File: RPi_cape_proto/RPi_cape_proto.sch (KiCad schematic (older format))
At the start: 78 parts, among them J1 Conn_01x04, J10 Conn_01x02, J11 Conn_01x02, J12 Conn_01x02, J15 Conn_01x06, J16 Conn_01x06, J2 Conn_02x20_Odd_Even, J21 Conn_01x06, J3 Conn_01x02, J4 Conn_01x02, J5 Conn_02x20_Odd_Even, J7 Conn_01x02, J8 Conn_02x20_Odd_Even, J9 Conn_01x02, Q2 MMBT3904, Q3 MMBT3904, U2 ADC128D818, U3 ADC128D818

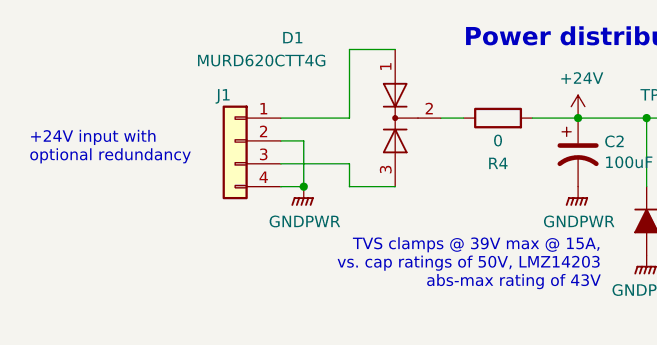
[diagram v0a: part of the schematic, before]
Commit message: Input ORing-diode details
Changed part number and improved heatsinking for input power OR-ing diode
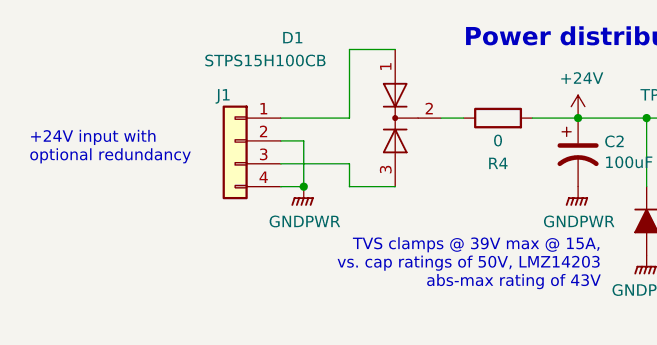
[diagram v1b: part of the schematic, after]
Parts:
- D1: value MURD620CTT4G -> STPS15H100CB; Manufacturer ON Semiconductor -> ST; Part Number MURD620CTT4G -> STPS15H100CB
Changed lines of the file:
@@
 F2 "In_RPi" I L 13850 7950 50
 F3 "In_CPLD" I L 13850 8050 50
-F5 "~Bat_On" O L 13850 7600 50
+F4 "~Bat_On" O L 13850 7600 50
 $EndSheet
 $Comp
@@
 P 2150 950
 F 0 "D1" V 1800 1350 50  0000 L CNN
-F 1 "MURD620CTT4G" V 1900 1250 50  0000 L CNN
+F 1 "STPS15H100CB" V 1900 1250 50  0000 L CNN
 F 2 "Package_TO_SOT_SMD:TO-252-2" H 2150 950 50  0001 C CNN
 F 3 "~" H 2150 950 50  0001 C CNN
-F 4 "ON Semiconductor" V 2150 950 50  0001 C CNN "Manufacturer"
-F 5 "MURD620CTT4G" V 2150 950 50  0001 C CNN "Part Number"
+F 4 "ST" V 2150 950 50  0001 C CNN "Manufacturer"
+F 5 "STPS15H100CB" V 2150 950 50  0001 C CNN "Part Number"
 	1    2150 950
 	0    -1   1    0

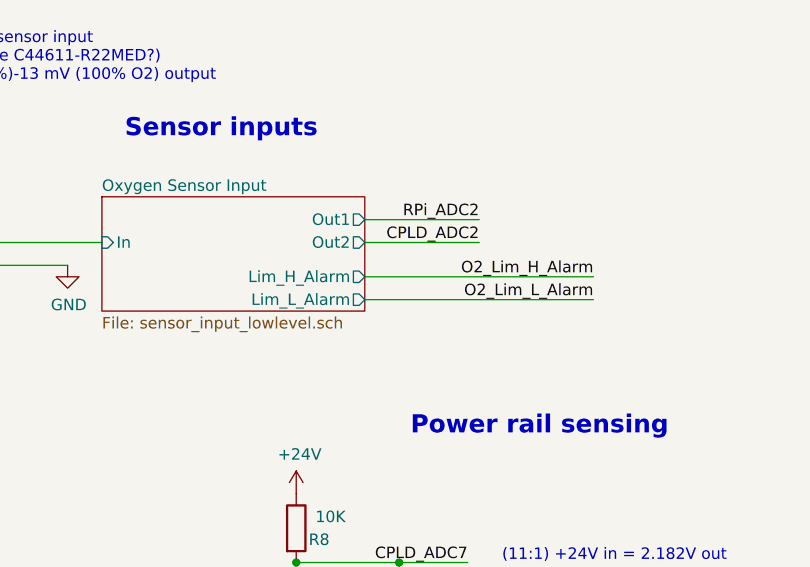
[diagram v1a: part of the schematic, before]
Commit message: Cleanup, manufacturing
Added doc on differences between 'proto' version and 'full' version
Added manufacturing README in proto version
Removed unused hardwired-limited O2 alarm nets in proto version
Fixed missed-annotation on D1 in full version
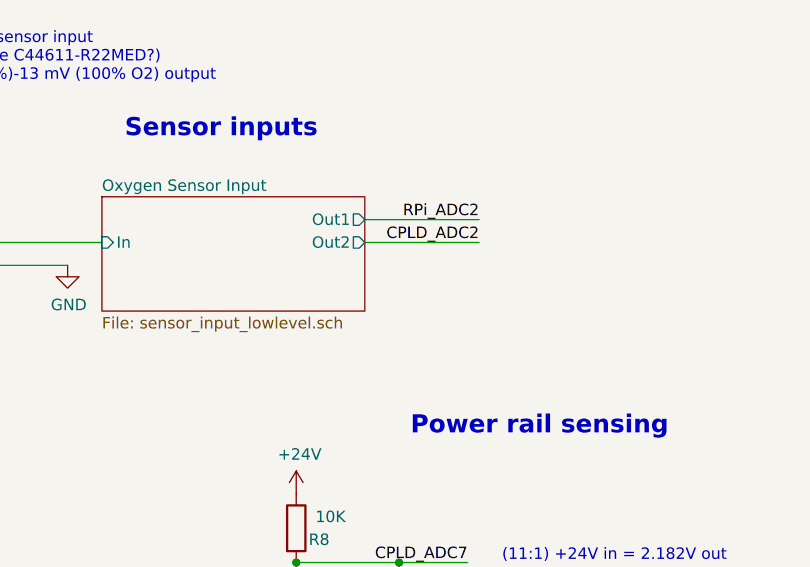
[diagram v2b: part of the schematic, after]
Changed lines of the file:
@@
 F3 "Out1" O R 2550 8200 50
 F4 "Out2" O R 2550 8300 50
-F5 "Lim_H_Alarm" O R 2550 8450 50
-F6 "Lim_L_Alarm" O R 2550 8550 50
 $EndSheet
 $Sheet
@@
 Text Label 10300 2550 0    50   ~ 0
 RPi_SCL
-Text Label 3550 8450 2    50   ~ 0
-O2_Lim_H_Alarm
-Text Label 3550 8550 2    50   ~ 0
-O2_Lim_L_Alarm
-Wire Wire Line
-	2550 8450 3550 8450
-Wire Wire Line
-	2550 8550 3550 8550
 Wire Wire Line
 	8750 7900 7950 7900

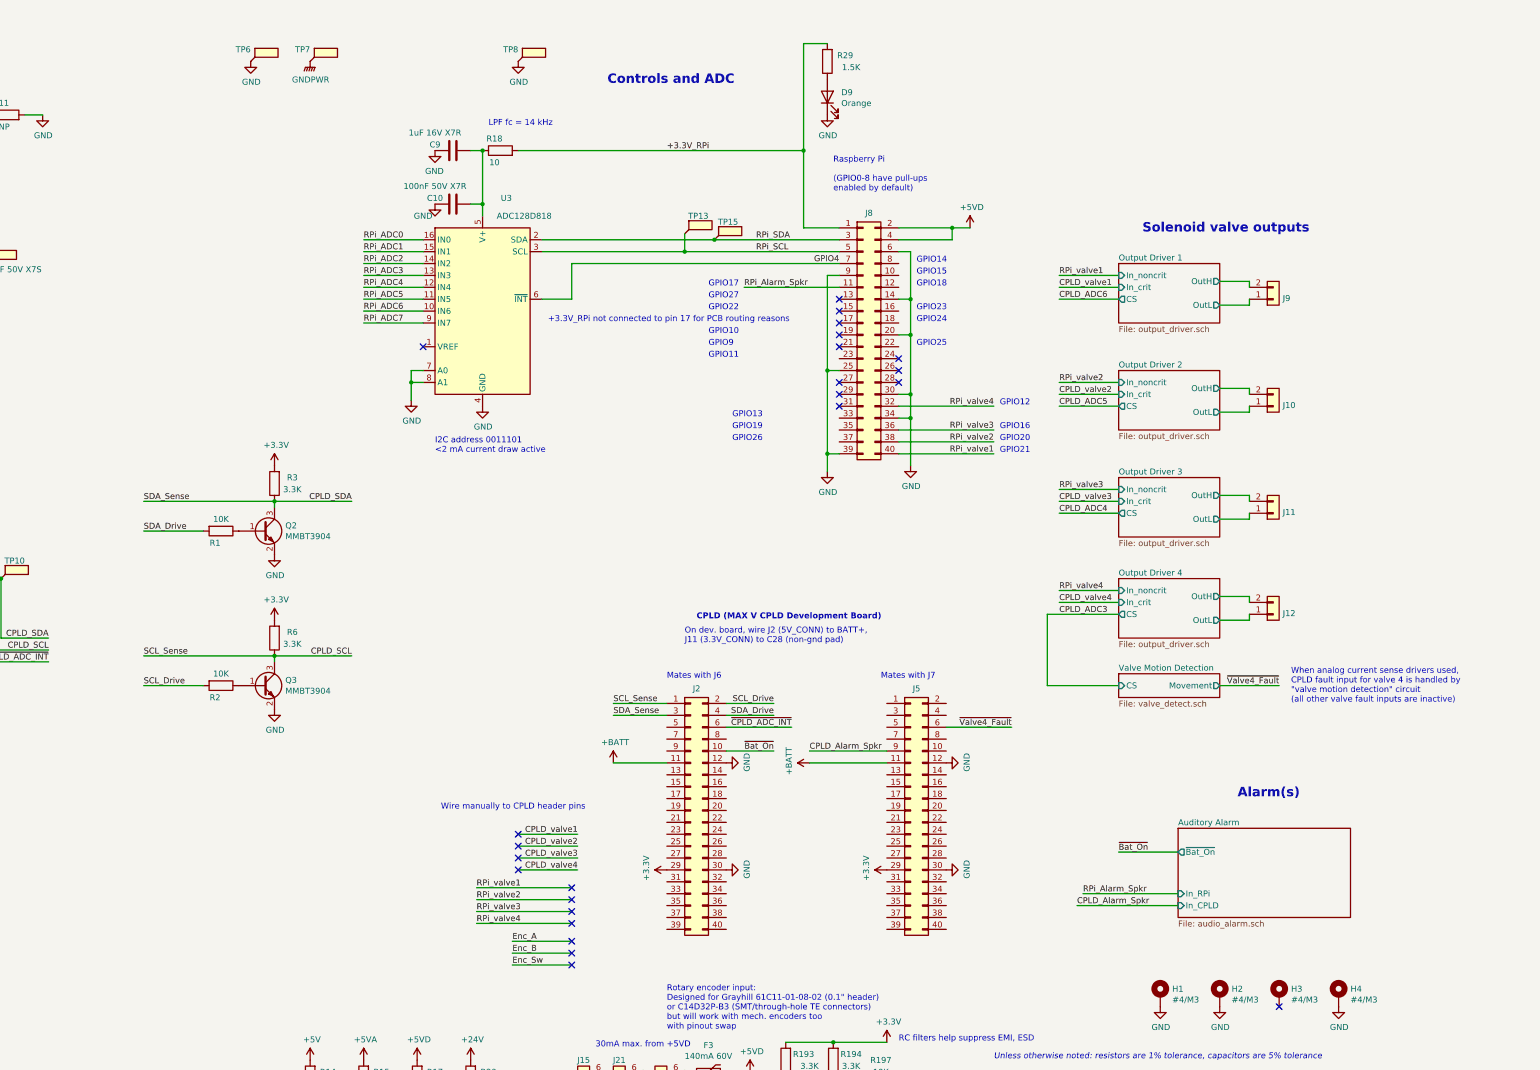
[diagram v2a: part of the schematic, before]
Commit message: Admin (licensing, naming)
Put under CERN open hardware license
Changed name to GlobalVent
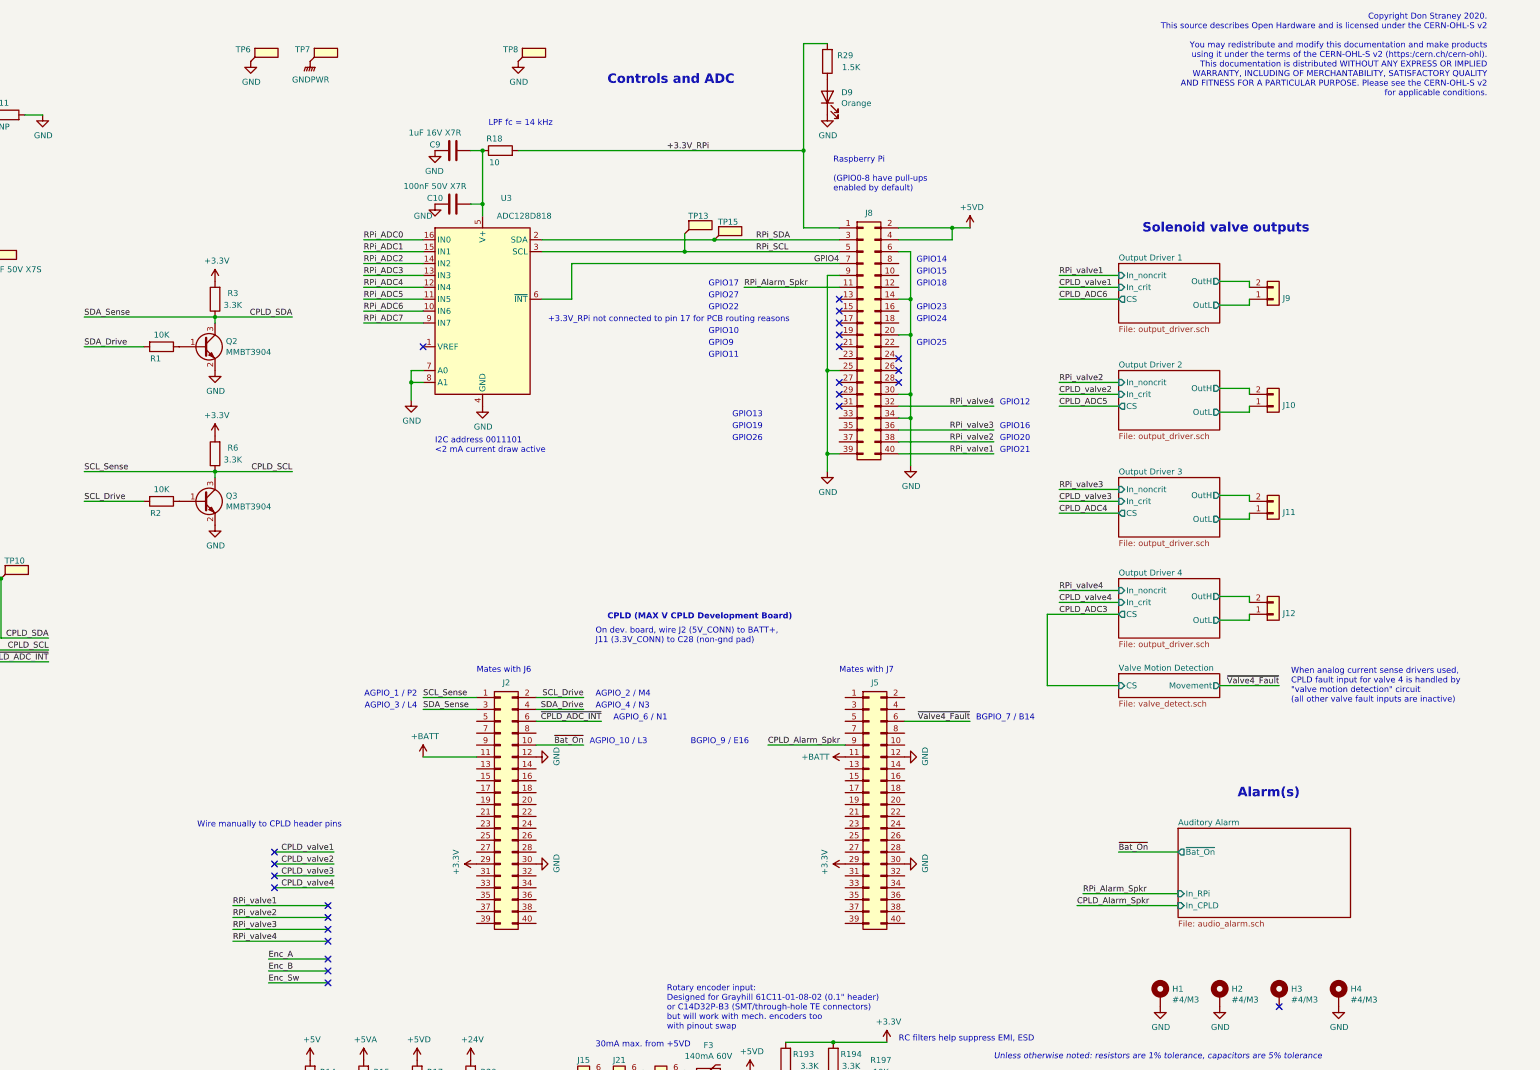
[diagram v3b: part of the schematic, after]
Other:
- note added: "AGPIO_1 / P2"
- note added: "AGPIO_10 / L3"
- note added: "AGPIO_2 / M4"
- note added: "AGPIO_3 / L4"
- note added: "AGPIO_4 / N3"
- note added: "AGPIO_6 / N1"
- note added: "BGPIO_7 / B14"
- note added: "BGPIO_9 / E16"
- note added: "Copyright Don Straney 2020.\nThis source describes Open Hardware and is licensed under the CERN-OHL-S v2\n\nYou may redistribute and modify this documentation and make products\nusing it under the terms of the CERN-OHL-S v2 (https:/cern.ch/cern-ohl).\nThis documentation is distributed WITHOUT ANY EXPRESS OR IMPLIED\nWARRANTY, INCLUDING OF MERCHANTABILITY, SATISFACTORY QUALITY\nAND FITNESS FOR A P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"
- moved on the sheet: J2, J5, Q2, Q3, R1, R2, R3, R6
